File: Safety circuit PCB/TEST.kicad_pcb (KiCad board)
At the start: 2 copper layers, 85.3 x 48.1 mm, 34 parts, among them J1 1053131202, J3 DT13-12PA-B016, Q1 2N7002K, Q2 2N7002K, Q3 2N7002K, Q4 2N7002K, Q5 2N7002K, Q6 2N7002K, Q7 2N7002K

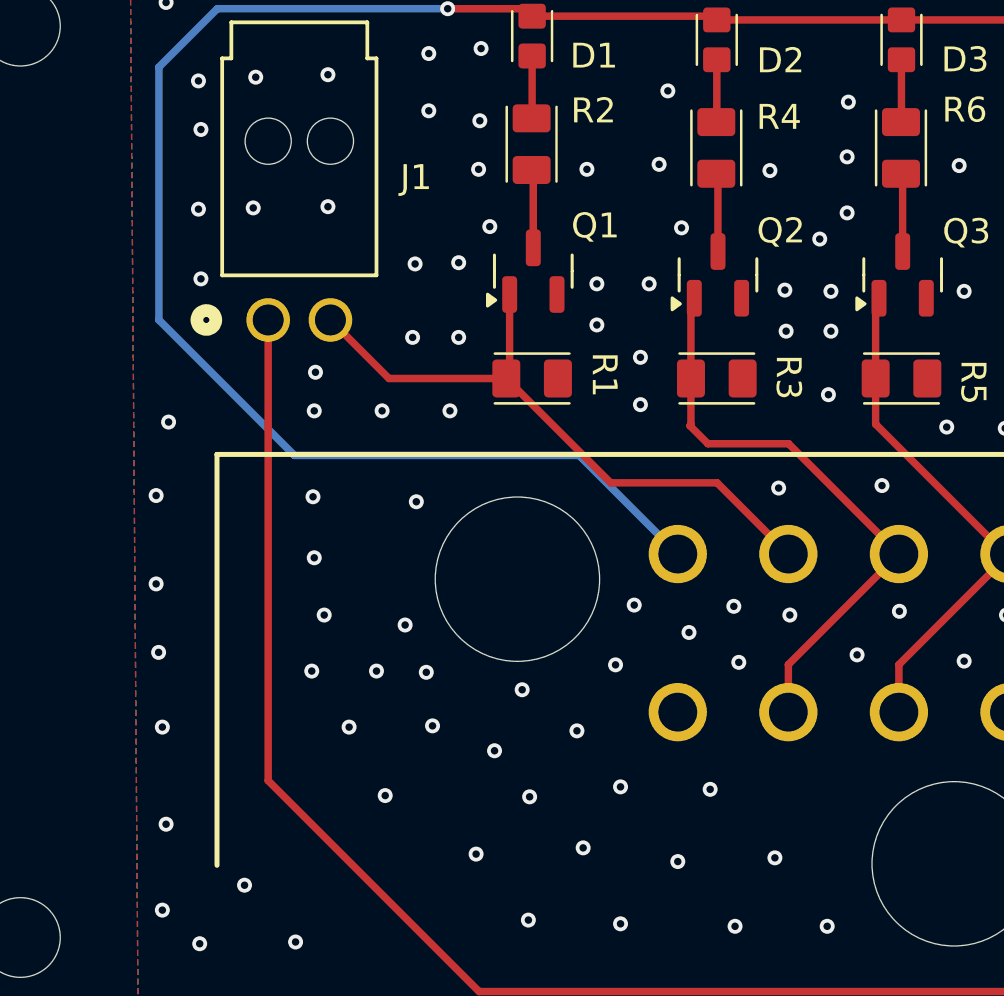
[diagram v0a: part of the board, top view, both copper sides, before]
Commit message: Add some more descriptive drawings to back silkscreen
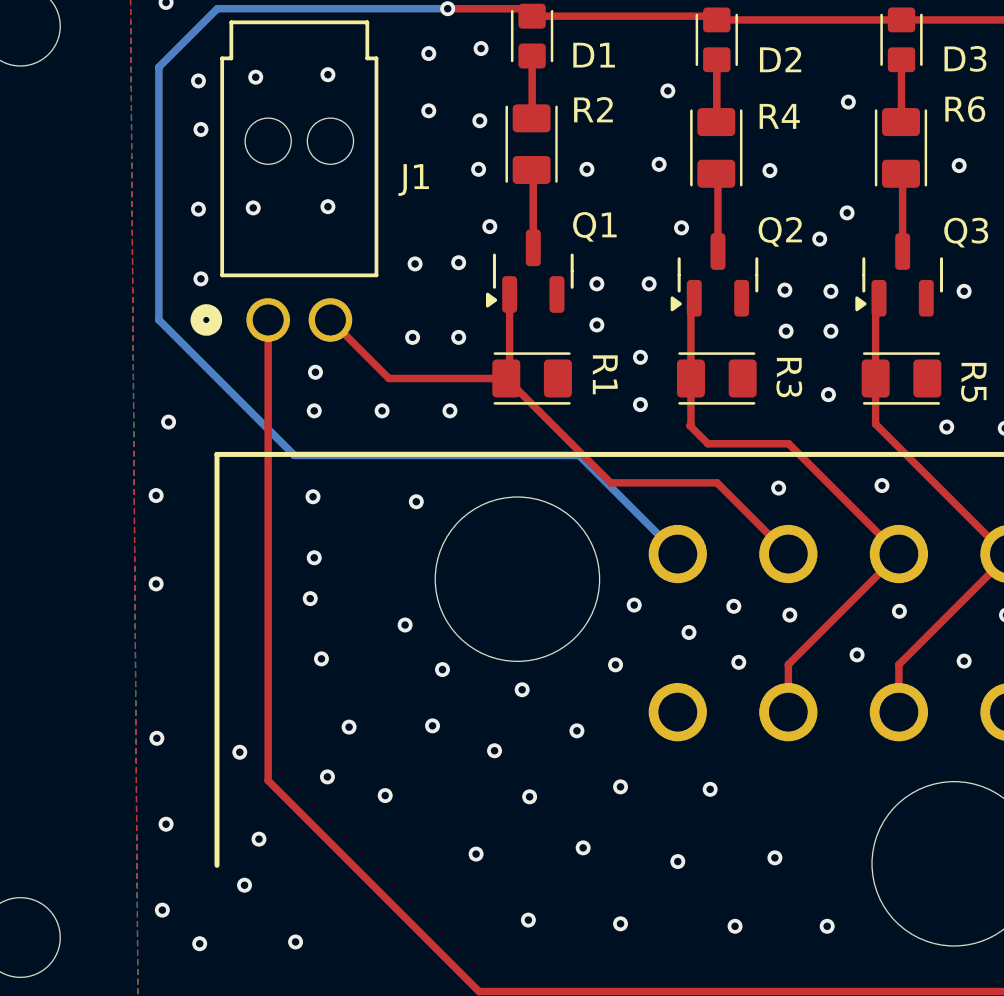
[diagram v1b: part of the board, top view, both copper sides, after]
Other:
- board text added: "FROM"
- board text added: "TO"
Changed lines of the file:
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@@
+		(layer "B.SilkS")
+	)
+	(gr_line
+		(start 130.86 67.98)
+		(end 134.438074 64.59)
+		(stroke
+			(width 0.1)
+			(type default)
+		)
 		(layer "B.SilkS")
 	)
@@
 		(layer "B.SilkS")
 	)
+	(gr_line
+		(start 135.554037 67.98)
+		(end 139.204037 64.59)
+		(stroke
+			(width 0.1)
+			(type default)
+		)
+		(layer "B.SilkS")
+	)
 	(gr_circle
 		(center 130.3 64.59)
@@
 		(layer "B.SilkS")
 	)
+	(gr_line
+		(start 125.85 67.98)
+		(end 129.744037 64.59)
+		(stroke
+			(width 0.1)
+			(type default)
+		)
+		(layer "B.SilkS")
+	)
 	(gr_circle
 		(center 134.998074 67.98)
@@
 		)
 		(fill no)
+		(layer "B.SilkS")
+	)
+	(gr_line
+		(start 140.32 67.98)
+		(end 143.834037 64.59)
+		(stroke
+			(width 0.1)
+			(type default)
+		)
 		(layer "B.SilkS")
 	)
@@
 		)
 	)
+	(gr_text "LB_S"
+		(at 111.83 88.14 0)
+		(layer "B.SilkS")
+		(effects
+			(font
+				(size 1 1)
+				(thickness 0.1)
+			)
+			(justify left bottom mirror)
+		)
+	)
 	(gr_text "1"
 		(at 145.55 60.08 0)
@@
 		)
 	)
+	(gr_text "FROM"
+		(at 104.84 86.1 0)
+		(layer "B.SilkS")
+		(effects
+			(font
+				(size 1 1)
+				(thickness 0.1)
+			)
+			(justify left bottom mirror)
+		)
+	)
 	(gr_text "8"
 		(at 125.01 73.16 0)
@@
 		)
 	)
+	(gr_text "TO\n"
+		(at 110.74 86.28 0)
+		(layer "B.SilkS")
+		(effects
+			(font
+				(size 1 1)
+				(thickness 0.1)
+			)
+			(justify left bottom mirror)
+		)
+	)
 	(gr_text "11"
 		(at 139.79 73.16 0)
@@
 	(gr_text "LB_S"
 		(at 126.88 62.64 0)
+		(layer "B.SilkS")
+		(effects
+			(font
+				(size 1 1)
+				(thickness 0.1)
+			)
+			(justify left bottom mirror)
+		)
+	)
+	(gr_text "BOTS_E"
+		(at 105.57 87.79 0)
 		(layer "B.SilkS")
 		(effects
@@
 	)
 	(via
-		(at 107.8 84.35)
+		(at 107.24 83.69)
 		(size 0.6)
 		(drill 0.3)
@@
 	)
 	(via
+		(at 107.93 90.85)
+		(size 0.6)
+		(drill 0.3)
+		(layers "F.Cu" "B.Cu")
+		(free yes)
+		(net 6)
+	)
+	(via
 		(at 158.5 79.75)
 		(size 0.6)
@@
 	)
 	(via
-		(at 101.3 88.85)
+		(at 101.08 89.3)
 		(size 0.6)
 		(drill 0.3)
@@
 	)
 	(via
+		(at 105.18 93.35)
+		(size 0.6)
+		(drill 0.3)
+		(layers "F.Cu" "B.Cu")
+		(free yes)
+		(net 6)
+	)
+	(via
 		(at 112 64.1)
 		(size 0.6)
@@
 	)
 	(via
-		(at 107.3 86.6)
+		(at 107.69 86.11)
 		(size 0.6)
 		(drill 0.3)
@@
 	)
 	(via
+		(at 104.41 89.86)
+		(size 0.6)
+		(drill 0.3)
+		(layers "F.Cu" "B.Cu")
+		(free yes)
+		(net 6)
+	)
+	(via
 		(at 121.6 63.3)
 		(size 0.6)
@@
 	)
 	(via
-		(at 109.9 86.6)
-		(size 0.6)
-		(drill 0.3)
-		(layers "F.Cu" "B.Cu")
-		(free yes)
-		(net 6)
-	)
-	(via
 		(at 113.9 93.95)
 		(size 0.6)
@@
 	)
 	(via
-		(at 128.8 65.95)
-		(size 0.6)
-		(drill 0.3)
-		(layers "F.Cu" "B.Cu")
-		(free yes)
-		(net 6)
-	)
-	(via
 		(at 101.55 76.6)
 		(size 0.6)
@@
 	)
 	(via
-		(at 101.15 85.85)
-		(size 0.6)
-		(drill 0.3)
-		(layers "F.Cu" "B.Cu")
-		(free yes)
-		(net 6)
-	)
-	(via
 		(at 128.15 71.35)
 		(size 0.6)
@@
 	)
 	(via
-		(at 111.9 86.65)
-		(size 0.6)
-		(drill 0.3)
+		(at 112.55 86.54)
+		(size 0.6)
+		(drill 0.3)

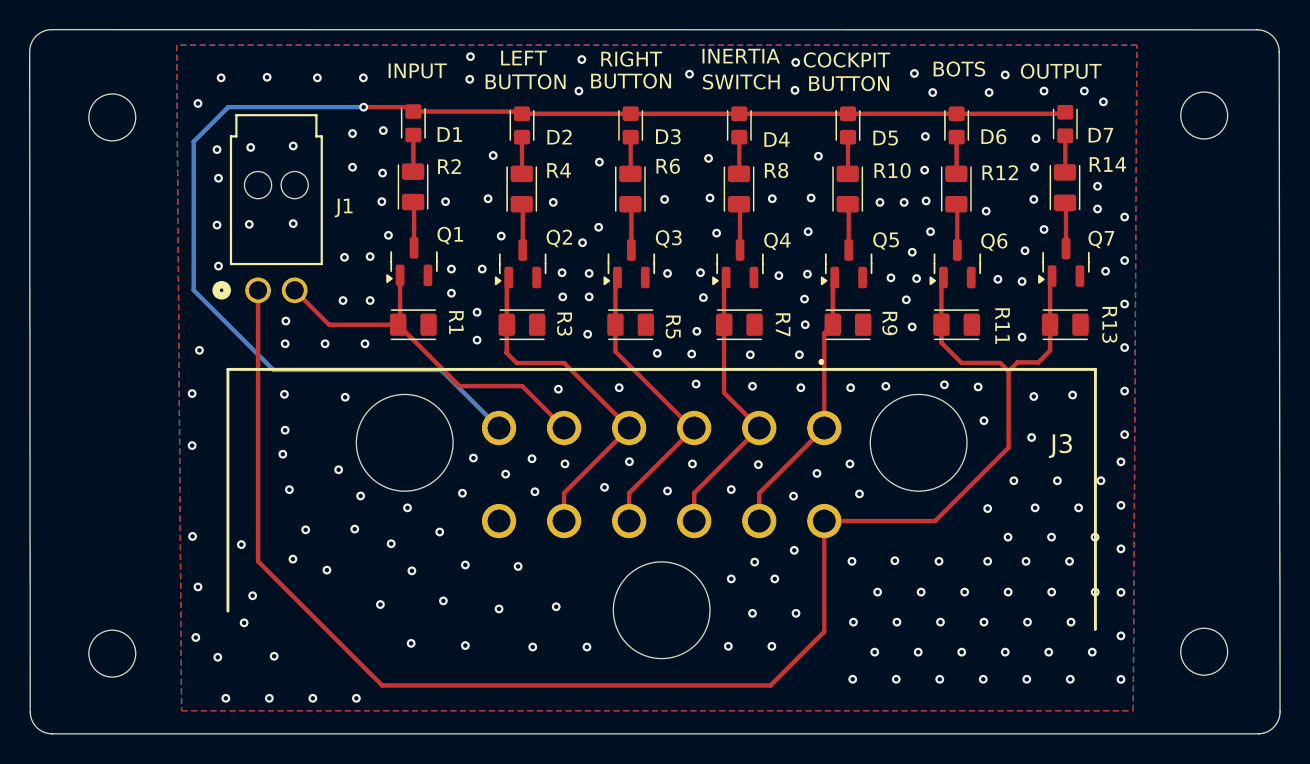
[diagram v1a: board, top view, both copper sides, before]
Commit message: Remove pull down resistors at MOSFET gates and increase sizes of traces
Also some more nice via tracing.
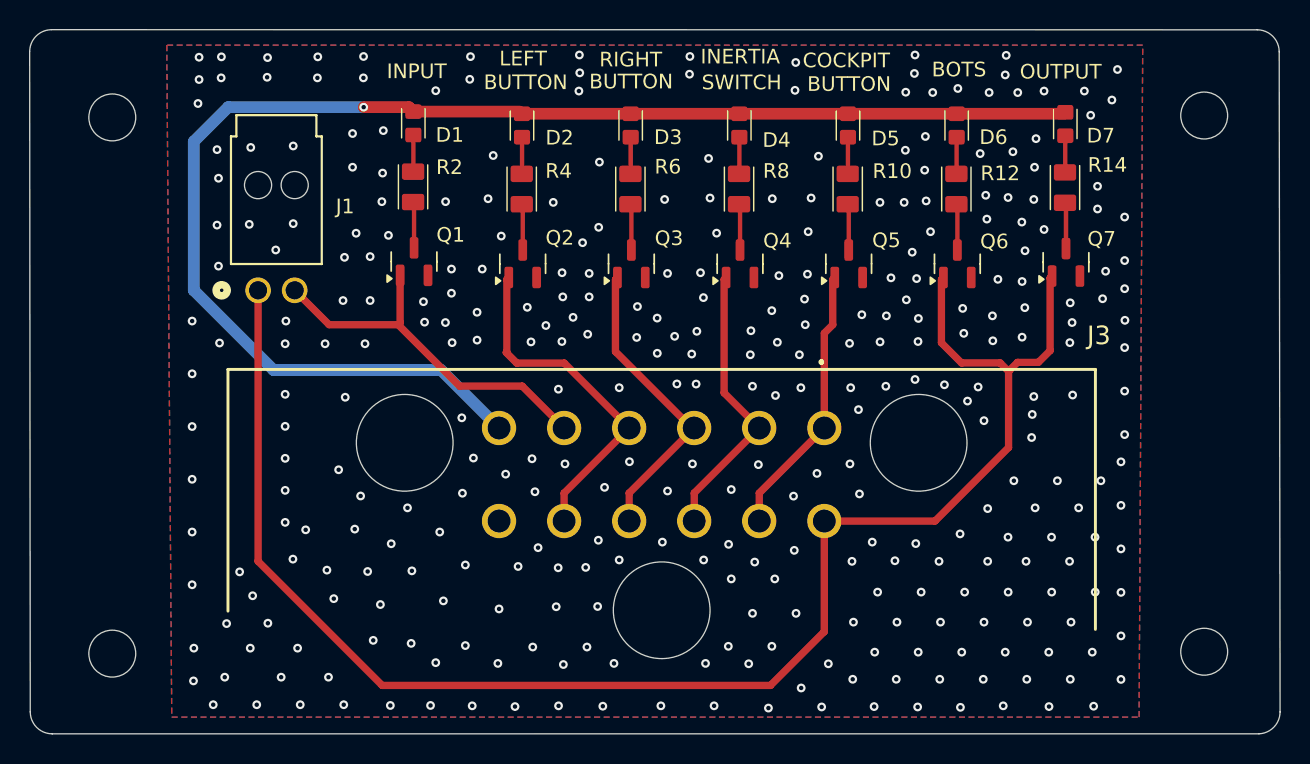
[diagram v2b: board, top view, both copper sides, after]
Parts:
- removed R1, R11, R13, R3, R5, R7, R9: 100k, SC:CRCW0805
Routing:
- net GND: vias 230 -> 339

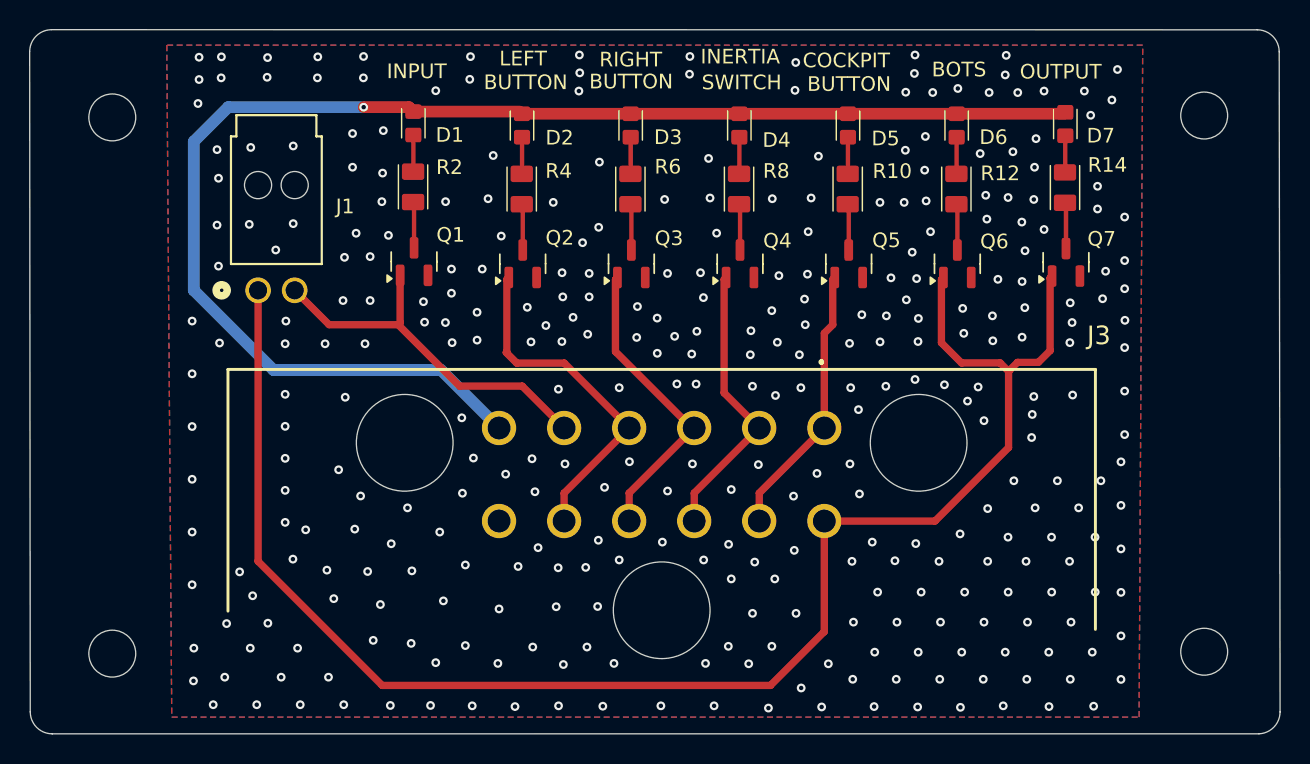
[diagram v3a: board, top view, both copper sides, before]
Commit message: 12-Pin connector changed to Molex Nano
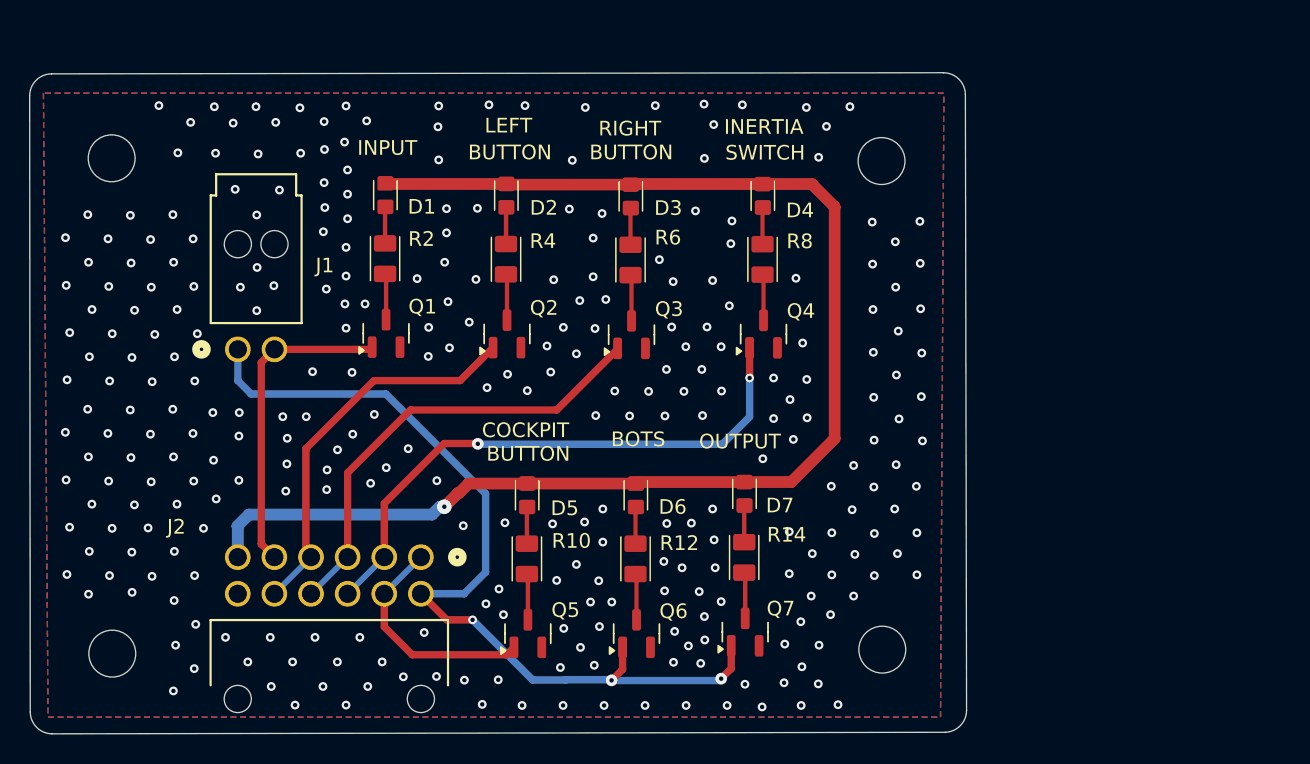
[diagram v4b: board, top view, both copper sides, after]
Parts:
- removed J3: DT13-12PA-B016, SC:DT1312PAB016
- added J2: 1053141312, SC:CONN_SD-105314-100_12_MOL, F.Cu at (116.7, 90.7)
- moved D7 33.4 mm to (138.8, 86.4)
- moved R10 33.4 mm to (123.9, 90.8)
- moved R14 33.4 mm to (138.7, 90.7)
- moved Q5 33.4 mm to (124.0, 95.9)
- moved Q6 33.4 mm to (131.4, 95.9)
- moved Q7 33.4 mm to (138.8, 95.8)
- moved R12 33.4 mm to (131.3, 90.8)
- moved D5 33.4 mm to (123.9, 86.5)
- moved D6 33.4 mm to (131.3, 86.5)
- moved REF** 22.2 mm to (148.1, 63.7)
- moved REF** 22.0 mm to (148.2, 97.0)
- moved Q1 5.26 mm to (114.3, 75.4)
- moved R2 5.26 mm to (114.2, 70.3)
- moved D1 5.26 mm to (114.2, 66.0)
- moved D4 5.06 mm to (140.0, 66.1)
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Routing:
- net /BOTS_END: track 108.1 -> 60.7 mm, vias 0 -> 3
- net /COCKPIT_BUTTON_START: track 19.5 -> 39.3 mm, vias 0 -> 2
- net /INERTIA_SWITCH_START: track 20.7 -> 31.2 mm
- net /INPUT: track 25.7 -> 21.7 mm
- net /BOTS_START: track 18.8 -> 15.6 mm
- net +12V: track 95.2 -> 92.2 mm
- net /LEFT_BUTTON_END: track 23.9 -> 26.2 mm
- net GND: vias 339 -> 300
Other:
- board size 85.3 x 48.1 mm -> 63.9 x 45.1 mm
